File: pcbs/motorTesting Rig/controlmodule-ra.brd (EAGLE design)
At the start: 76.2 x 50.8 mm, 31 parts, among them Q1 16mhz, U1 ATMEGA328P_TQFP

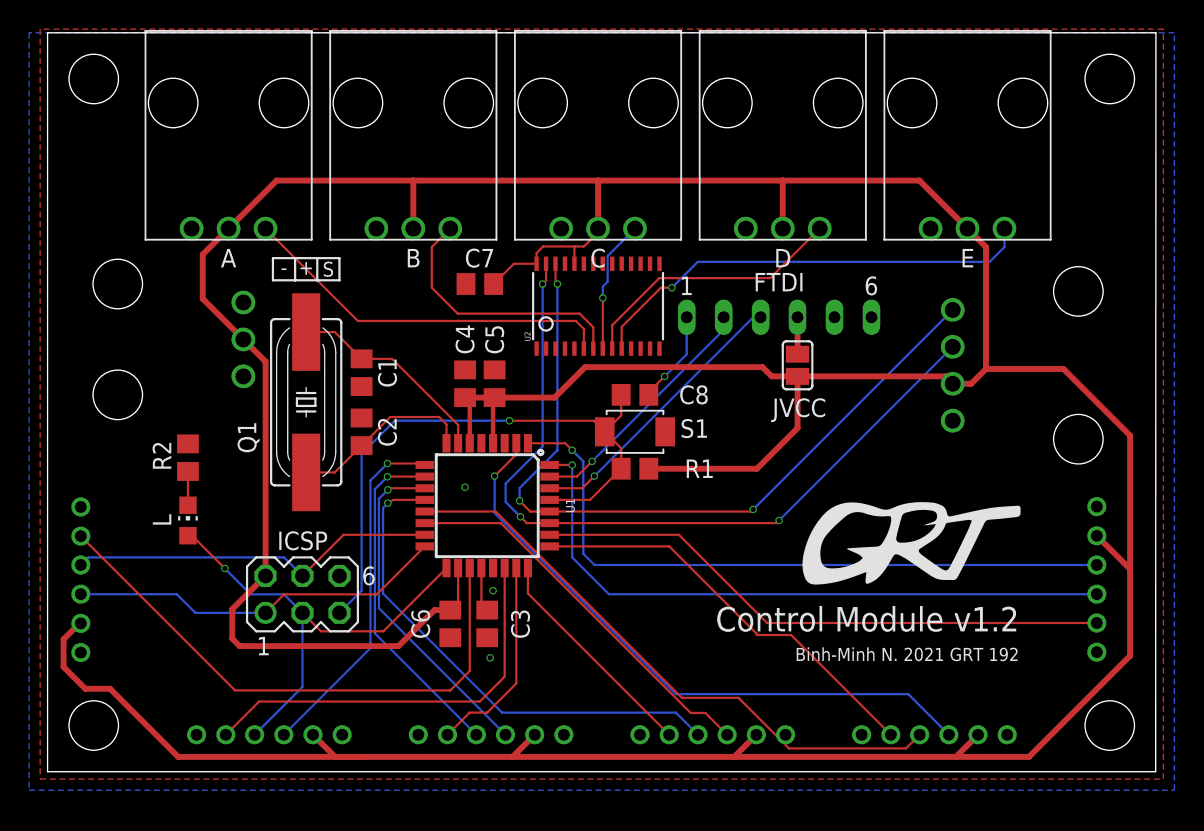
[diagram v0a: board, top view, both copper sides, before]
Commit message: control board v1.3, moved stuff to bottom side to avoid aluminum shavings
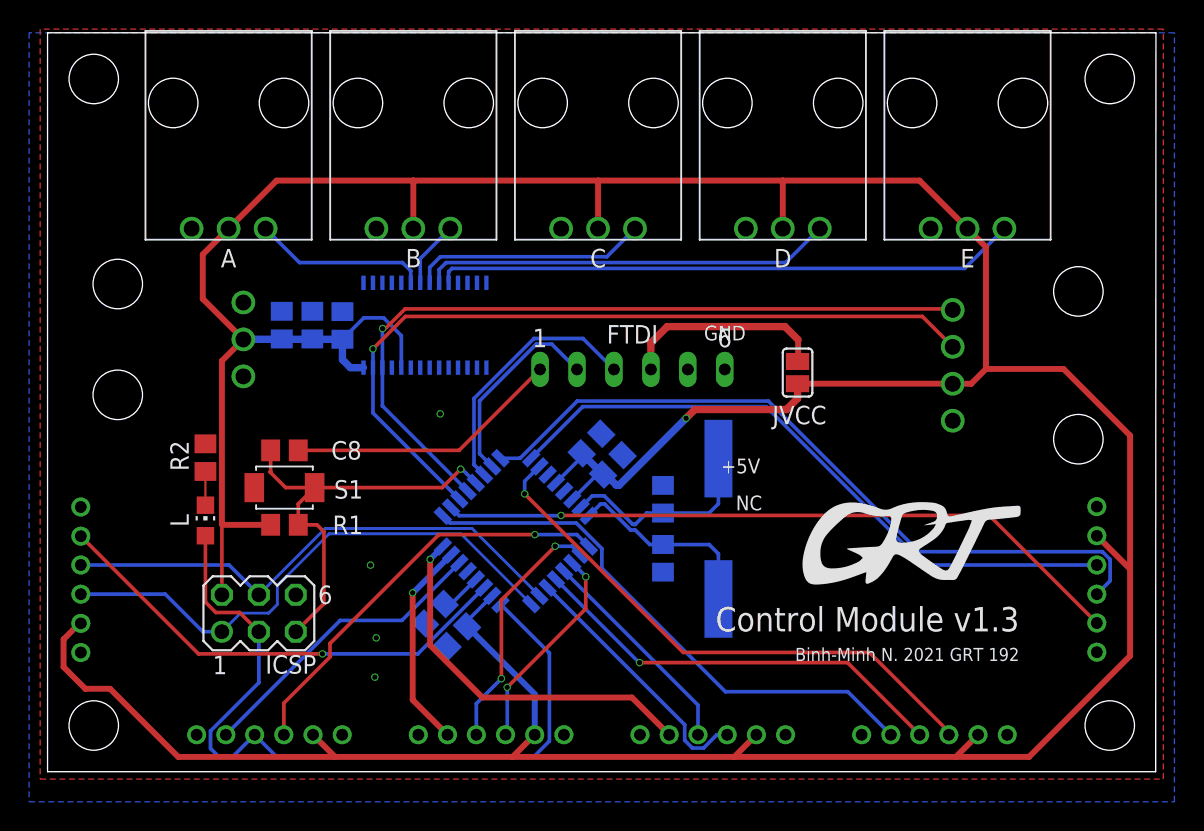
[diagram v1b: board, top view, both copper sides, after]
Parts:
- added C10: 10u, rcl:C0805
- added C9: 1u, rcl:C0805
- moved Q1 29.6 mm to (46.1, 16.7), flipped to the bottom
- moved R1 24.4 mm to (16.3, 17.0), turned to 180 degrees
- moved S1 24.4 mm to (16.3, 19.5), turned to 180 degrees
- moved C8 24.4 mm to (16.3, 22.1)
- moved C1 22.5 mm to (42.3, 18.7), flipped to the bottom, turned to 270 degrees
- moved C2 22.5 mm to (42.3, 14.7), flipped to the bottom, turned to 90 degrees
- moved U2 12.0 mm to (25.9, 30.7), flipped to the bottom, turned to 180 degrees
- moved C4 11.6 mm to (38.9, 21.1), flipped to the bottom, turned to 135 degrees
- moved FTDI 10.7 mm to (40.2, 27.7)
- moved C7 9.87 mm to (20.3, 30.7), flipped to the bottom, turned to 270 degrees
- moved C5 7.83 mm to (37.4, 22.6), flipped to the bottom, turned to 135 degrees
- moved C3 3.67 mm to (26.6, 10.9), flipped to the bottom, turned to 315 degrees
- moved ICSP 3.27 mm to (14.5, 10.9)
- moved U1 2.63 mm to (32.2, 16.5), flipped to the bottom, turned to 315 degrees
- moved L 1.20 mm to (10.9, 17.3)
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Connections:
- net XTAL1 renamed XTAL_P
- net XTAL2 renamed XTAL_N
- net GND: now also C10.1, C9.1
- net VCC: now also C10.2, C9.2
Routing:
- net VCC: track 317.1 -> 293.5 mm, vias 0 -> 1
- net SCK: track 32.0 -> 54.6 mm, vias 1 -> 0
- net ENC: track 34.6 -> 15.1 mm, vias 1 -> 0
- net PWM0: track 26.1 -> 12.0 mm
- net PWM1: track 18.3 -> 4.58 mm
- net N$9: track 6.41 -> 18.9 mm, vias 1 -> 0
- net N$1: track 2.54 -> 14.3 mm
- net END: track 41.2 -> 29.4 mm, vias 0 -> 1
- net RESET: track 41.4 -> 29.7 mm
- net MISO: track 26.1 -> 37.6 mm
- net POTC: track 15.5 -> 26.1 mm, vias 0 -> 1
- net MOSI: track 25.6 -> 36.2 mm
- net PWM3: track 18.6 -> 28.2 mm
- net POTD: track 28.9 -> 37.8 mm
- net REVC: track 26.8 -> 17.9 mm
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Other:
- board text added: "- + NC"
- board text added: "Control Module v1.3"
- board text removed: "Control Module v1.2"
